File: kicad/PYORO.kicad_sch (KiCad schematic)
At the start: 17 parts, among them J1 BM06B-SRSS-TBLFSN, J2 Conn_01x04_Pin, Q1 TEFT4300, U1 STM32H503CBTx, U2 L293D, U3 ICM-20948

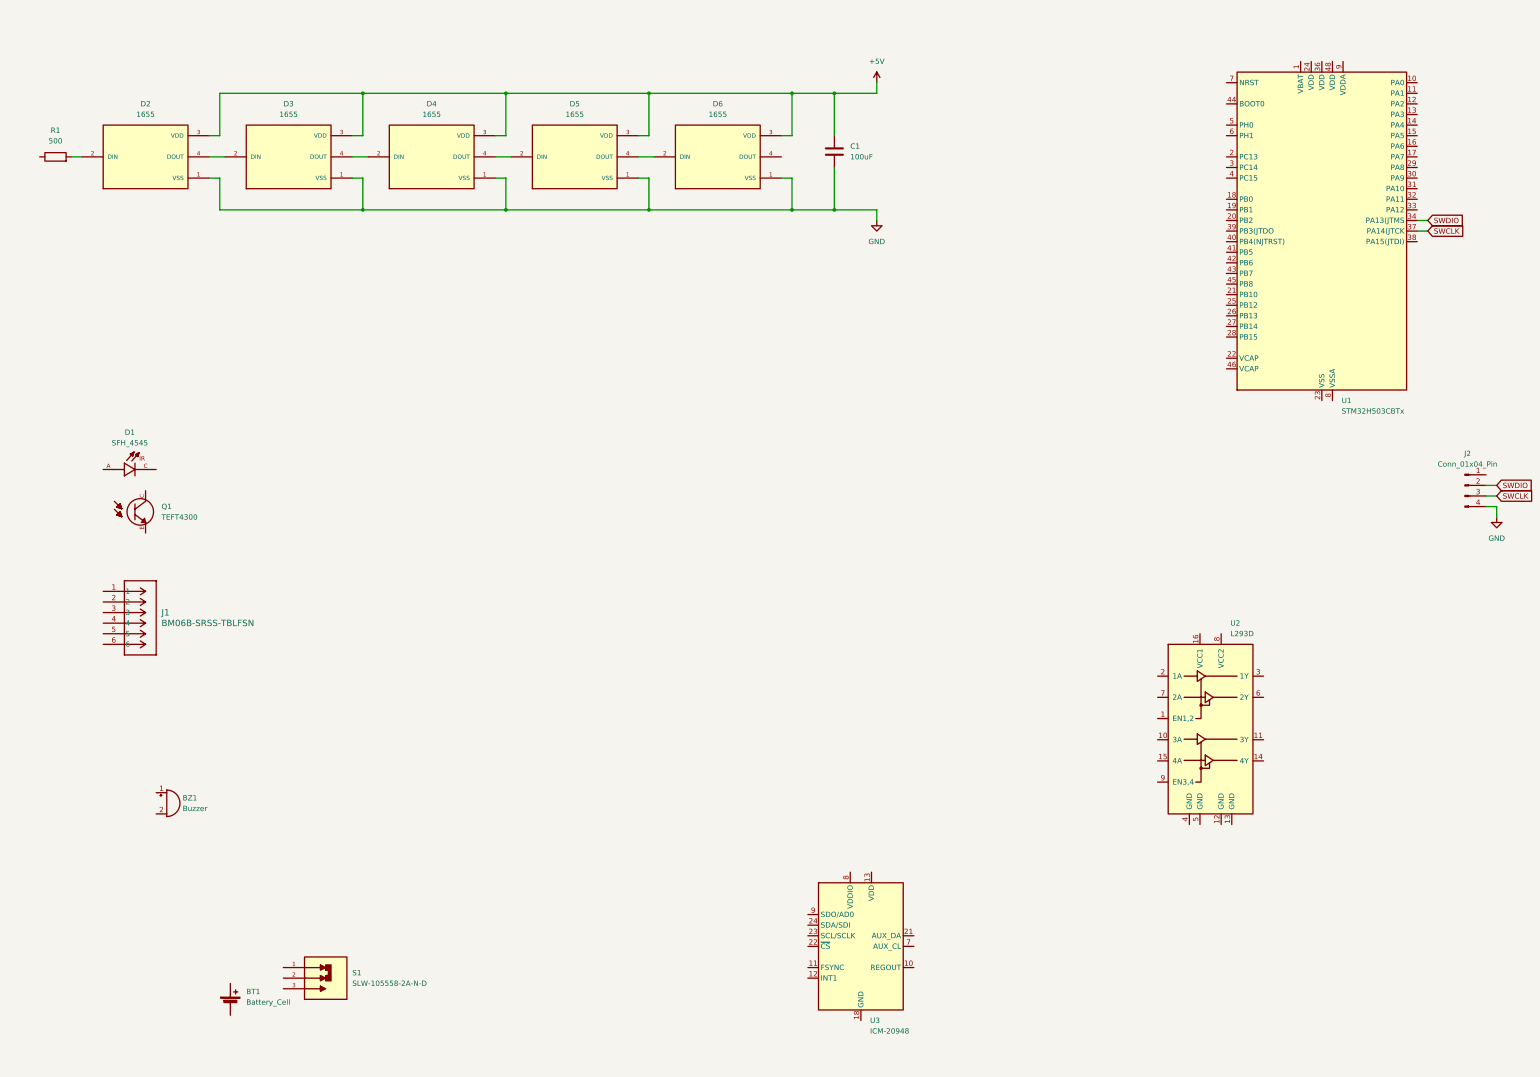
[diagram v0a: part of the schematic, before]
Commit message: Started IMU circuit
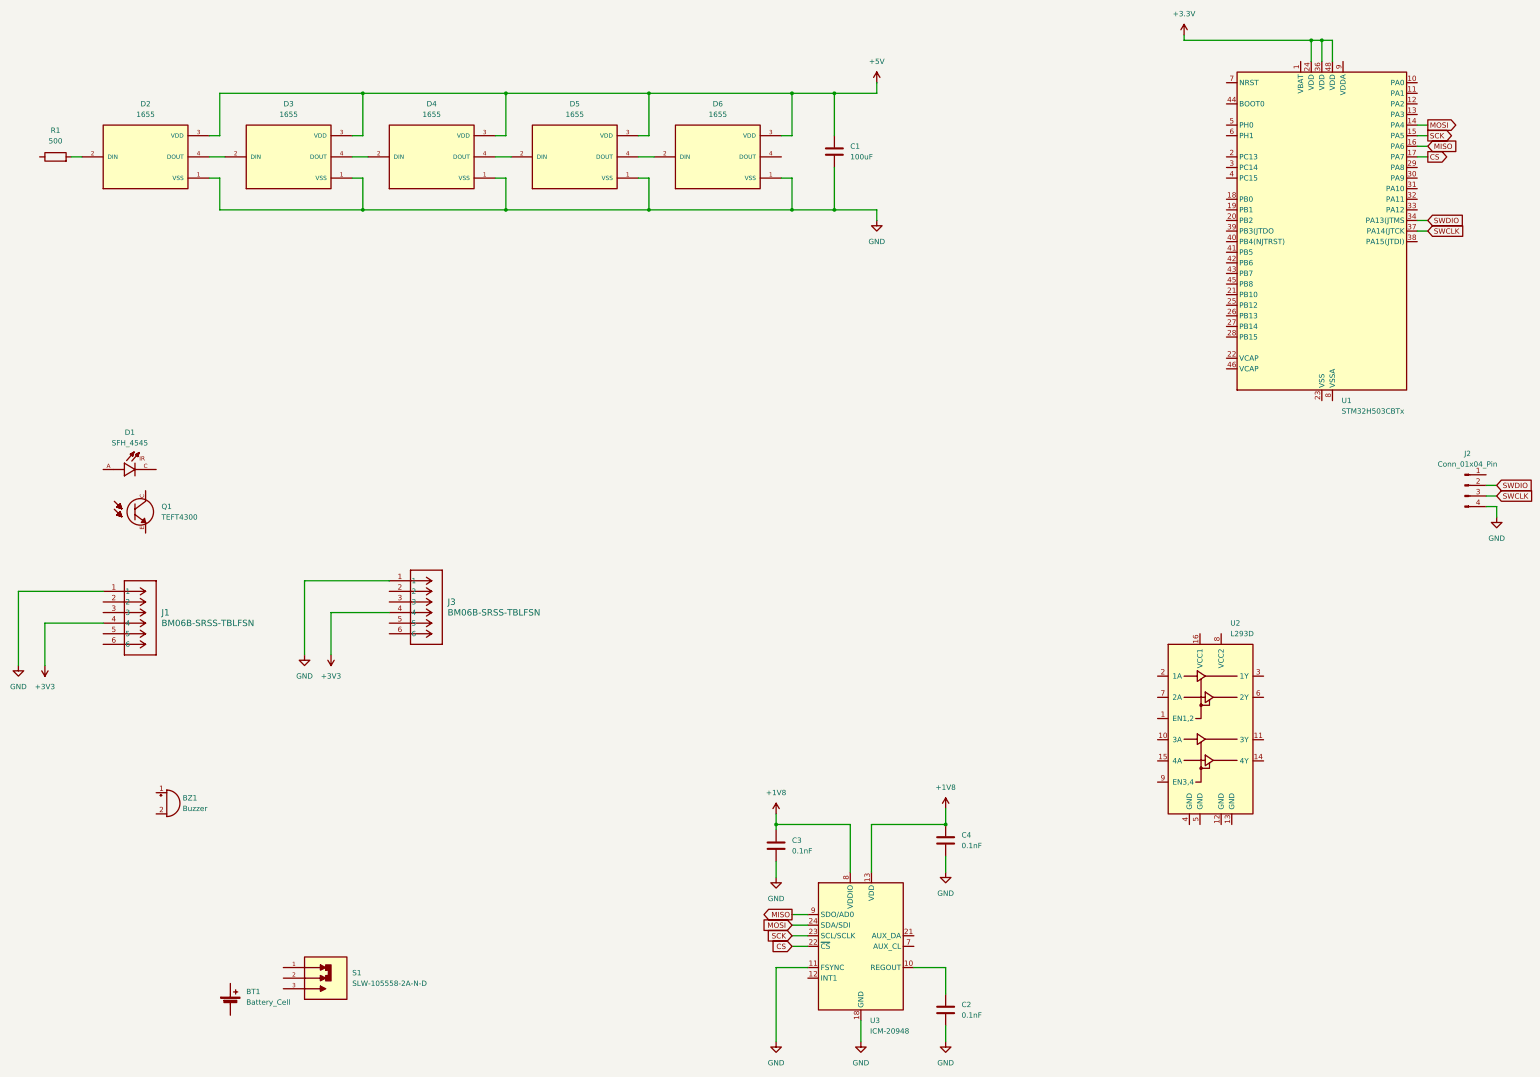
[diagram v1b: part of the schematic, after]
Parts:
- added C2, C3, C4: 0.1nF, symbol Device:C
- added J3: BM06B-SRSS-TBLFSN, BM06B_SRSS_TB_LF__SN_:CONN_BM06B-SRSS-TB_JST, symbol CONN_BM06B-SRSS-TB_JST:BM06B-SRSS-TBLFSN
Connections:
- net GND: now also J1.1, U3.11 (FSYNC), U3.18 (GND), U3.20 (GND), C2.2, C3.1, C4.1, J3.1
- net MOSI: now reaches U1.14 (PA4)
- net MOSI: now also U3.24 (SDA/SDI)
- net SCK: now reaches U1.15 (PA5)
- net SCK: now also U3.23 (SCL/SCLK)
- net MISO: now reaches U1.16 (PA6)
- net MISO: now also U3.9 (SDO/AD0)
- net CS: now reaches U1.17 (PA7)
- net CS: now also U3.22 (~{CS})
- net +3.3V: now reaches U1.24 (VDD)
- net +3.3V: now also U1.36 (VDD), U1.48 (VDD)
- net at U3.10 (REGOUT): now also C2.1
- net +1V8: now reaches U3.13 (VDD)
- net +1V8: now also U3.8 (VDDIO), C3.2, C4.2
- net +3V3: now reaches J1.4
- net +3V3: now also J3.4

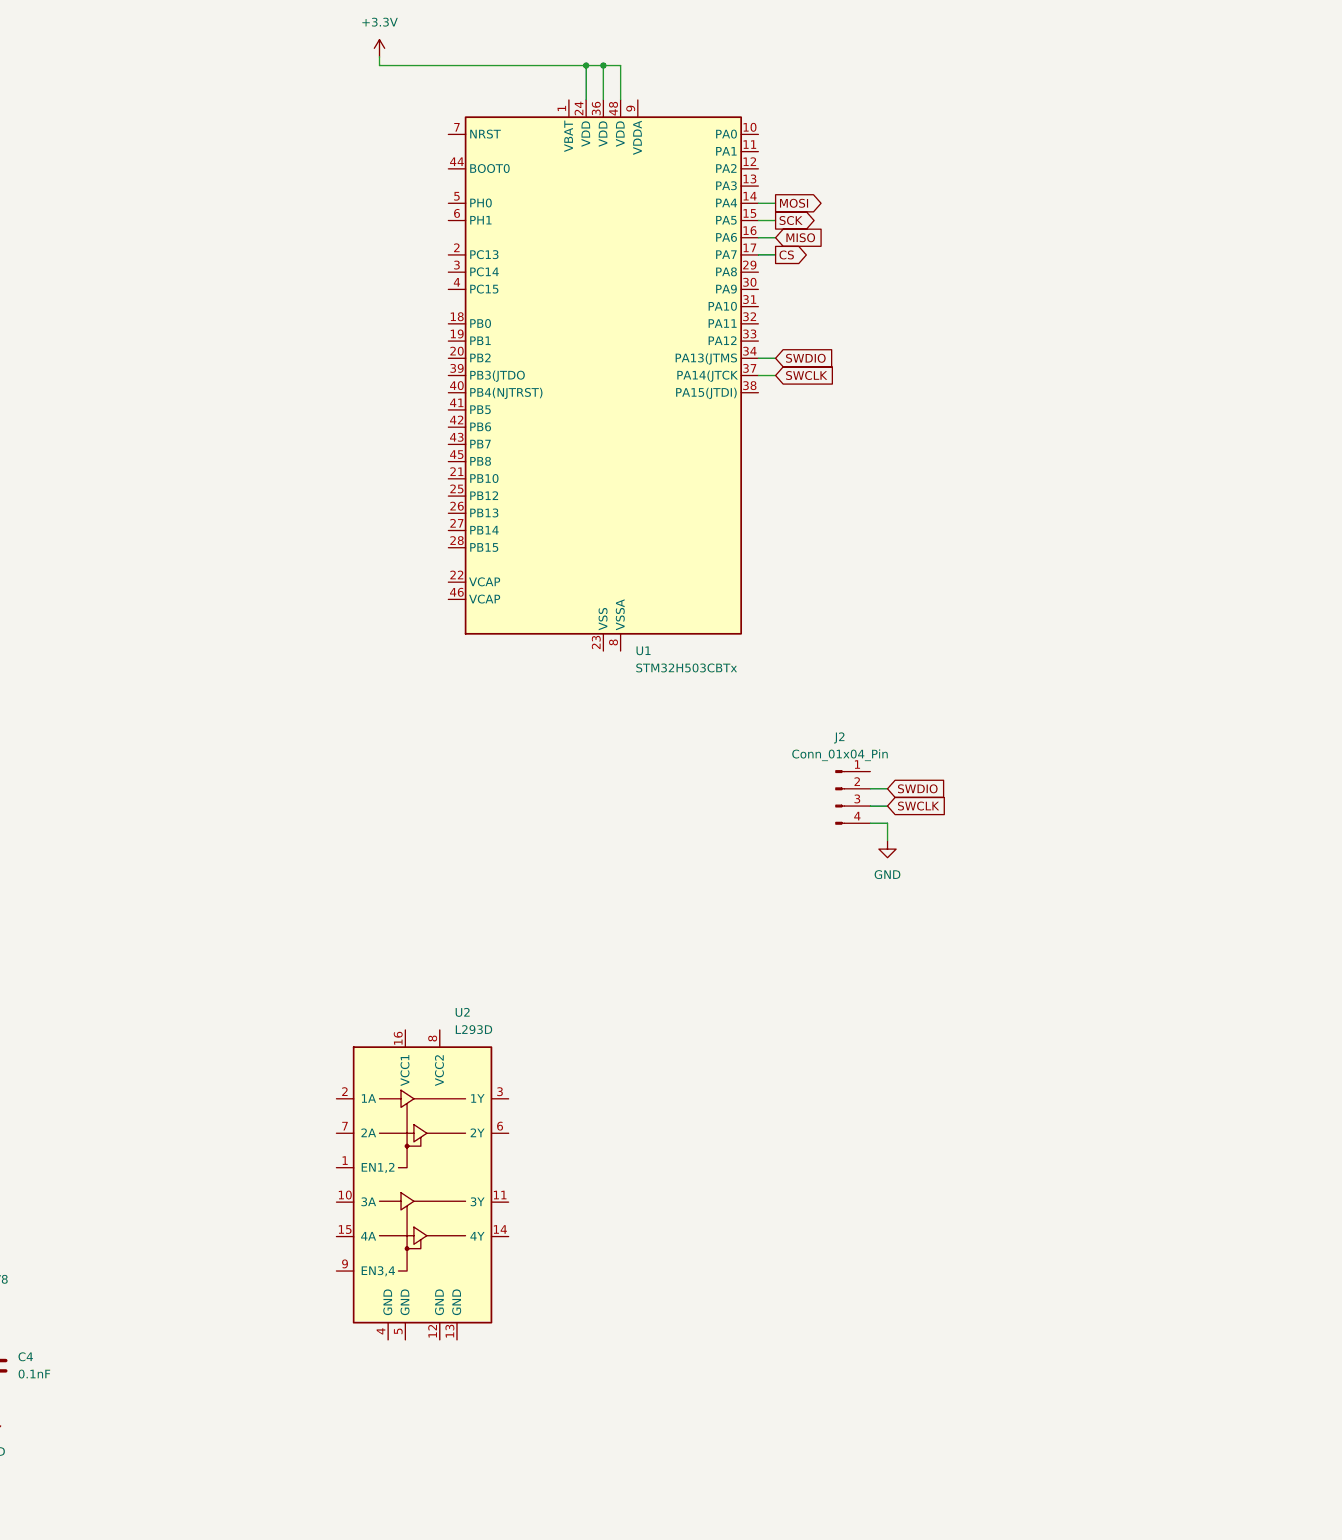
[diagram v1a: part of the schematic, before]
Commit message: Started motor controller
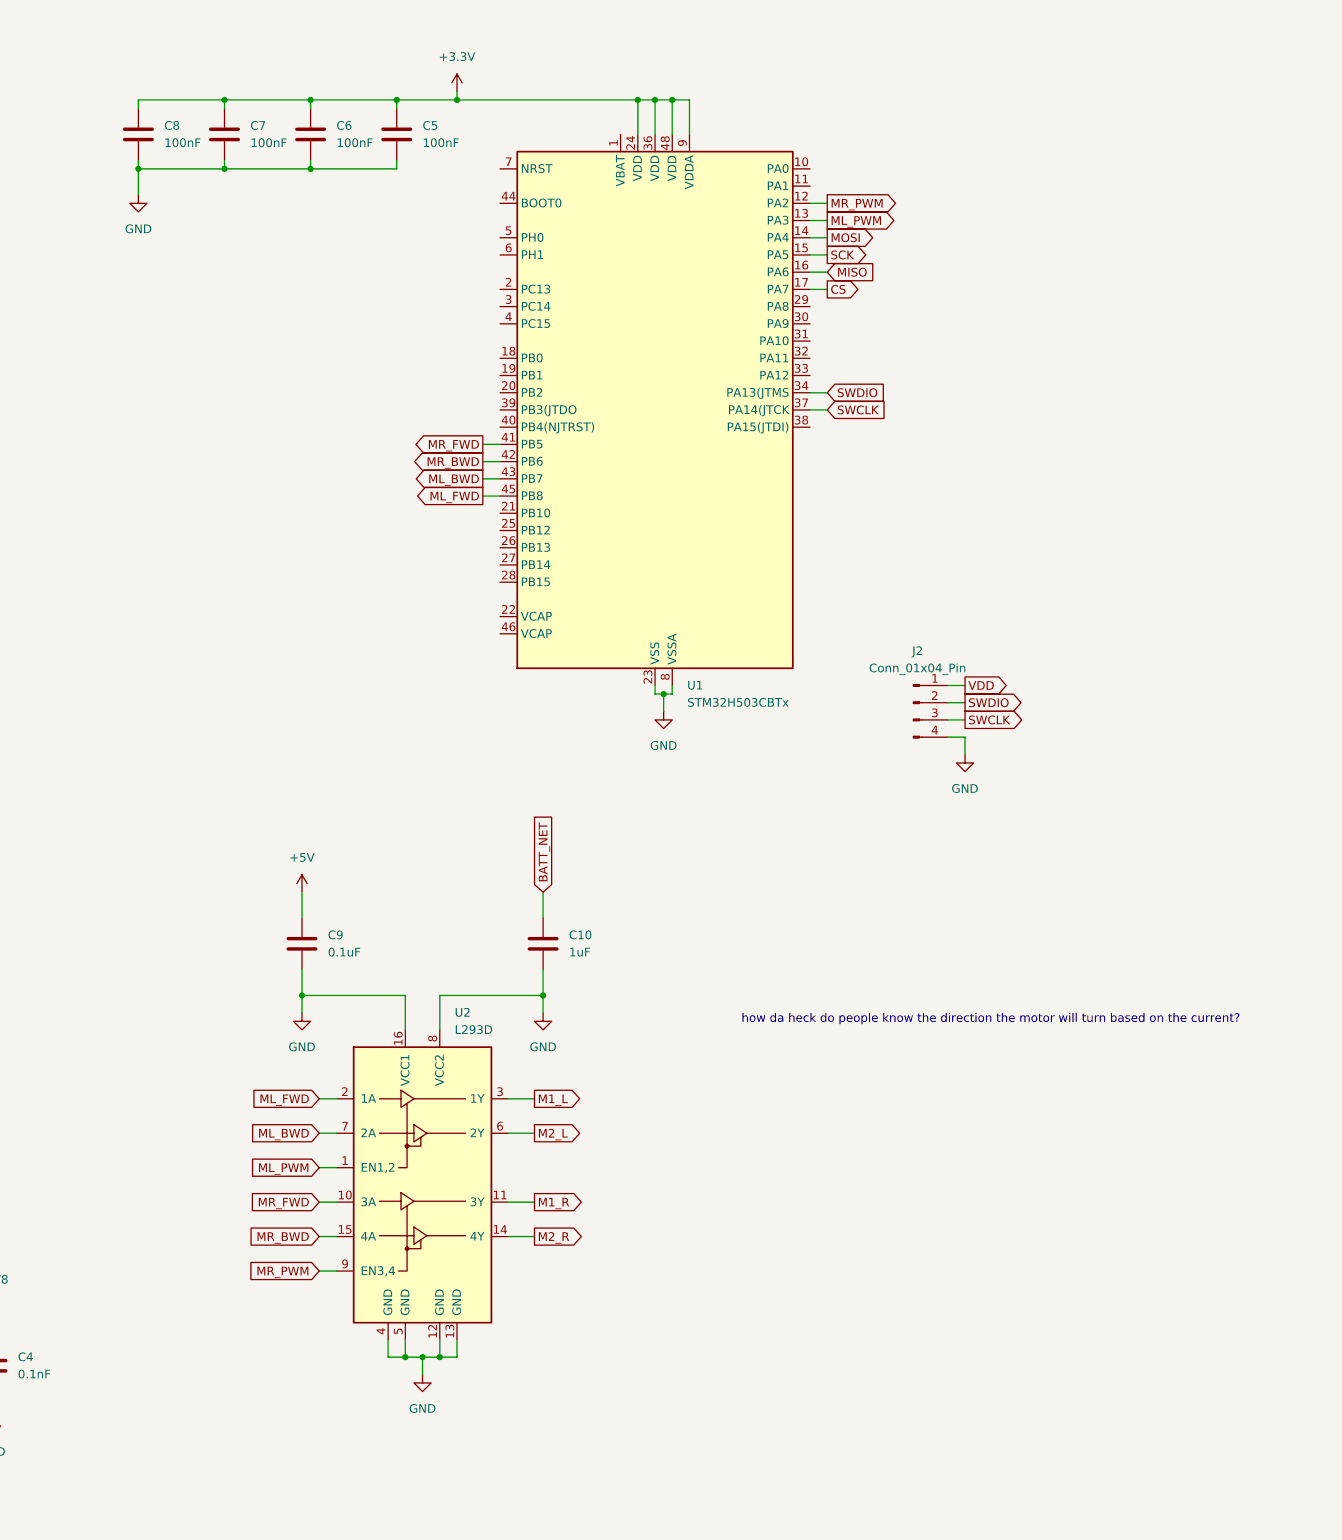
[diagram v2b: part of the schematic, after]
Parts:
- added C10: 1uF, symbol Device:C
- added C5, C6, C7, C8: 100nF, symbol Device:C
- added C9: 0.1uF, symbol Device:C
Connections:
- net +3.3V: now also U1.9 (VDDA), C5.1, C6.1, C7.1, C8.1
- net +5V: now also C9.1
- net GND: now also U1.23 (VSS), U1.35 (VSS), U1.47 (VSS), U1.8 (VSSA), U2.12 (GND), U2.13 (GND), U2.16 (VCC1), U2.4 (GND), U2.5 (GND), U2.8 (VCC2), C10.2, C5.2, C6.2, C7.2, C8.2, C9.2
- net MR_PWM: now reaches U1.12 (PA2)
- net MR_PWM: now also U2.9 (EN3,4)
- net ML_PWM: now reaches U1.13 (PA3)
- net ML_PWM: now also U2.1 (EN1,2)
- net MR_FWD: now reaches U1.41 (PB5)
- net MR_FWD: now also U2.10 (3A)
- net MR_BWD: now reaches U1.42 (PB6)
- net MR_BWD: now also U2.15 (4A)
- net ML_BWD: now reaches U1.43 (PB7)
- net ML_BWD: now also U2.7 (2A)
- net ML_FWD: now reaches U1.45 (PB8)
- net ML_FWD: now also U2.2 (1A)
- net VDD: now reaches J2.1 (Pin_1)
- net M1_R: now reaches U2.11 (3Y)
- net M2_R: now reaches U2.14 (4Y)
- net M1_L: now reaches U2.3 (1Y)
- net M2_L: now reaches U2.6 (2Y)
- new net BATT_NET: C10.1
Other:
- note added: "how da heck do people know the direction the motor will turn based on the current?"
- moved on the sheet: J2, U1

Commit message: Started 6-pin JST Headers
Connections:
- net M1_L: now also J1.6
- net M1_R: now also J3.6
- net M2_L: now also J1.5
- net M2_R: now also J3.5
- net ML_ENC_B: now reaches U1.10 (PA0)
- net ML_ENC_B: now also J1.2
- net ML_ENC_A: now reaches U1.11 (PA1)
- net ML_ENC_A: now also J1.3
- net MR_ENC_A: now reaches U1.21 (PB10)
- net MR_ENC_A: now also J3.3
- net MR_ENC_B: now reaches U1.28 (PB15)
- net MR_ENC_B: now also J3.2
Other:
- moved on the sheet: C10, C2, C3, C4, C9, J1, J3, U2, U3

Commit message: Started IR Receivers, and changed pin assignment
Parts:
- added Q2, Q3, Q4: TEFT4300, MM_Library:Emitter, symbol TEFT4300:TEFT4300
- added R2, R3, R4, R5: R, symbol Device:R
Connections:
- net +3.3V is gone; now on net +3V3: C5.1, C6.1, C7.1, C8.1, U1.24 (VDD), U1.36 (VDD), U1.48 (VDD), U1.9 (VDDA)
- net CS: now also U1.31 (PA10); no longer U1.17 (PA7)
- net ML_BWD: now also U1.40 (PB4(NJTRST)); no longer U1.43 (PB7)
- net SCK: now also U1.29 (PA8); no longer U1.15 (PA5)
- net RECIV_FR: now reaches U1.18 (PB0)
- net RECIV_FR: now also Q3.E, R4.1
- net RECIV_BR: now reaches U1.19 (PB1)
- net RECIV_BR: now also Q4.E, R5.1
- net +3.3VA: now reaches Q1.C
- net +3.3VA: now also Q2.C, Q3.C, Q4.C
- net RECIV_FL: now reaches Q1.E
- net RECIV_FL: now also U1.15 (PA5), R2.1
- new net AGND: R2.2, R3.2, R4.2, R5.2
- new net RECIV_BL: Q2.E, R3.1, U1.17 (PA7)
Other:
- moved on the sheet: BZ1, D1, Q1
